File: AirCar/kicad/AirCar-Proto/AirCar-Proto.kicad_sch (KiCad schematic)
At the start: 6 parts, among them J1 Conn_01x05, J2 Barrel_Jack, J3 Conn_01x05, SW1 SW_Push, SW2 SW_SPDT, U1 Pico

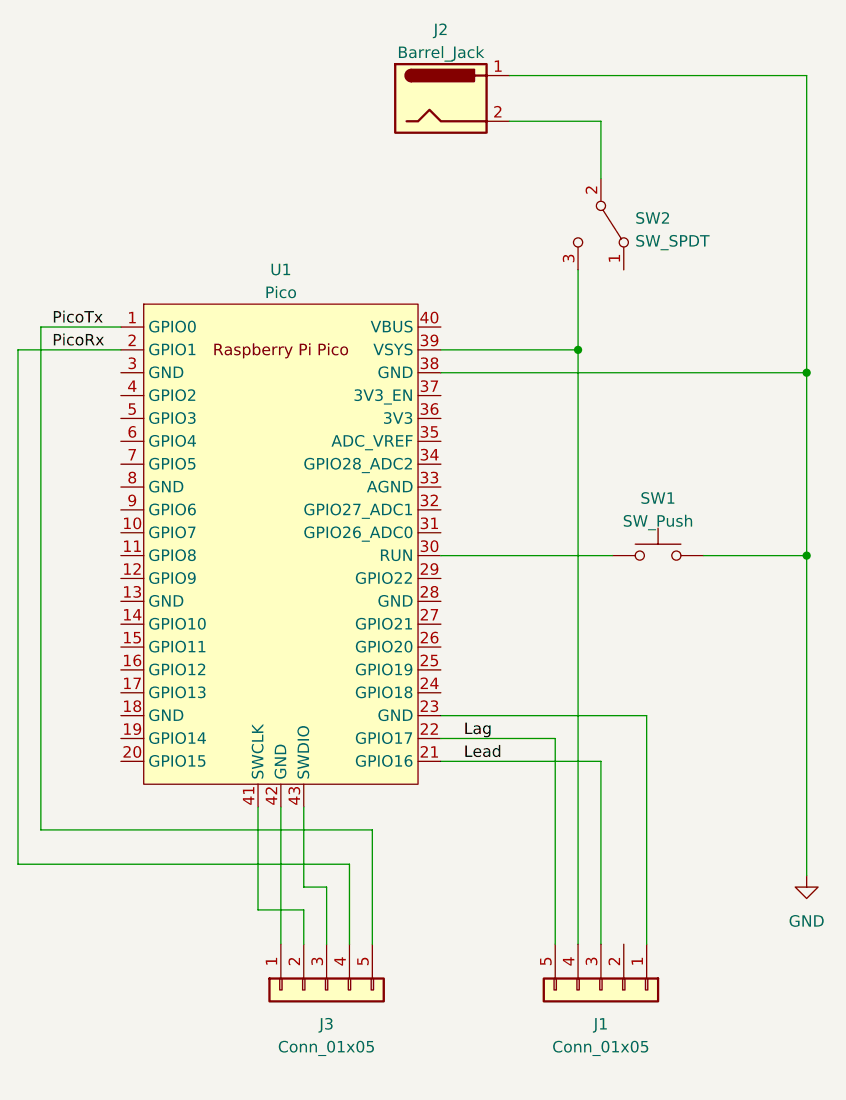
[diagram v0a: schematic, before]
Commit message: Add rudimentary schematic for proto-board version.
Note:  This schematic runs the rotary encoder below it's minimum
VDD value.  It seems to work fine (as it should), but it may be
flaky.

This fixes a bug in the stateUpdate logic that manifests when the
lead pin is higher (pin number) than the lag pin.
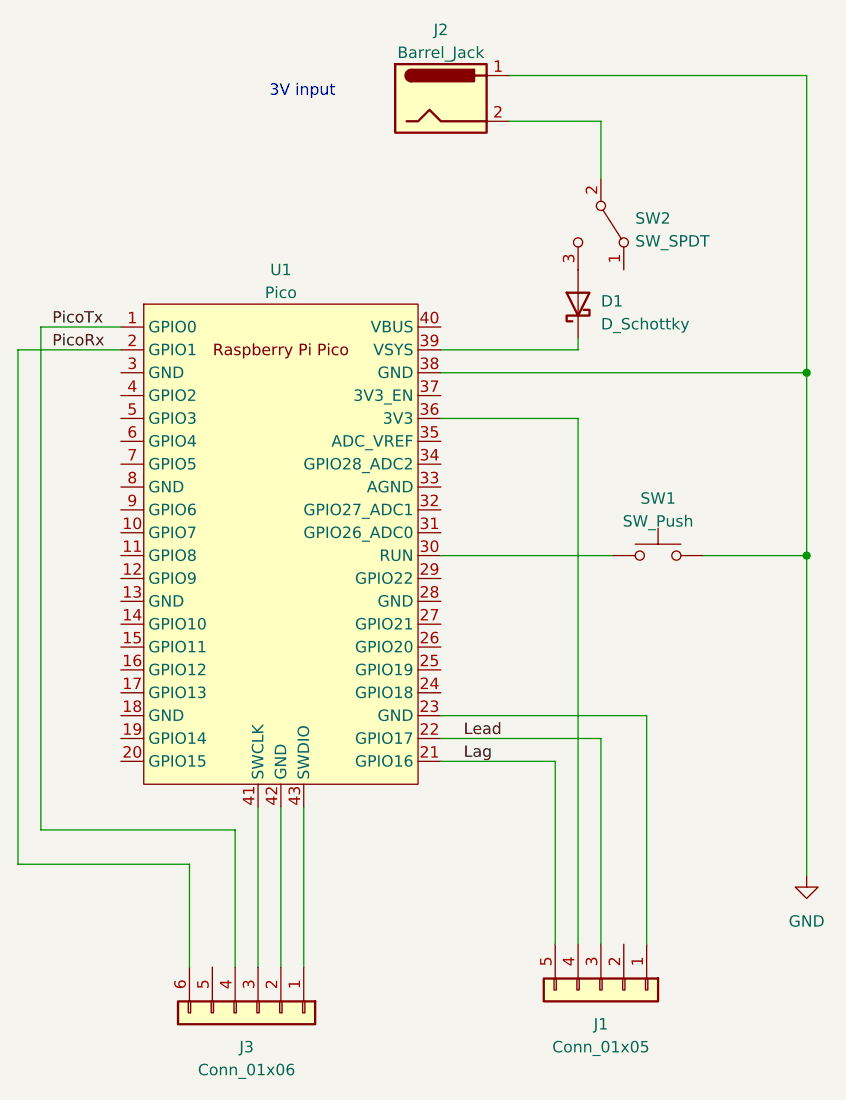
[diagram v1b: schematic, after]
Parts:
- removed J3: Conn_01x05, symbol Connector_Generic:Conn_01x05
- added D1: D_Schottky, symbol Device:D_Schottky
- added J3: Conn_01x06, symbol Connector_Generic:Conn_01x06
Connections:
- net Lag: now also U1.21 (GPIO16); no longer U1.22 (GPIO17)
- net Lead: now also U1.22 (GPIO17); no longer U1.21 (GPIO16)
- net PicoRx: now also J3.6 (Pin_6)
- net PicoTx: now also J3.4 (Pin_4)
- net at U1.36 (3V3): now also J1.4 (Pin_4)
- net at U1.41 (SWCLK): now also J3.3 (Pin_3)
- net at U1.42 (GND): now also J3.2 (Pin_2)
- net at U1.43 (SWDIO): now also J3.1 (Pin_1)
- new net: D1.2 (A), SW2.3 (C)
- new net: D1.1 (K), U1.39 (VSYS)
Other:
- note added: "3V input"
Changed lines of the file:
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@@
   (junction (at 236.22 83.82) (diameter 0) (color 0 0 0 0)
   )
-  (junction (at 210.82 60.96) (diameter 0) (color 0 0 0 0)
-  )
   (wire (pts (xy 213.36 35.56) (xy 213.36 41.91))
     (stroke (width 0) (type default))
   )
-  (wire (pts (xy 180.34 127) (xy 180.34 123.19))
-    (stroke (width 0) (type default))
-  )
-  (wire (pts (xy 180.34 123.19) (xy 175.26 123.19))
-    (stroke (width 0) (type default))
-  )
-  (wire (pts (xy 187.96 114.3) (xy 151.13 114.3))
-    (stroke (width 0) (type default))
-  )
-  (wire (pts (xy 182.88 120.65) (xy 180.34 120.65))
-    (stroke (width 0) (type default))
-  )
-  (wire (pts (xy 180.34 120.65) (xy 180.34 111.76))
+  (wire (pts (xy 195.58 106.68) (xy 208.28 106.68))
+    (stroke (width 0) (type default))
+  )
+  (wire (pts (xy 148.59 118.11) (xy 167.64 118.11))
+    (stroke (width 0) (type default))
+  )
+  (wire (pts (xy 180.34 111.76) (xy 180.34 129.54))
     (stroke (width 0) (type default))
   )
@@
     (stroke (width 0) (type default))
   )
-  (wire (pts (xy 187.96 127) (xy 187.96 114.3))
+  (wire (pts (xy 151.13 114.3) (xy 172.72 114.3))
     (stroke (width 0) (type default))
   )
@@
     (stroke (width 0) (type default))
   )
-  (wire (pts (xy 185.42 118.11) (xy 185.42 127))
-    (stroke (width 0) (type default))
-  )
   (wire (pts (xy 203.2 30.48) (xy 236.22 30.48))
     (stroke (width 0) (type default))
@@
     (stroke (width 0) (type default))
   )
-  (wire (pts (xy 213.36 127) (xy 213.36 106.68))
-    (stroke (width 0) (type default))
-  )
-  (wire (pts (xy 175.26 123.19) (xy 175.26 111.76))
-    (stroke (width 0) (type default))
-  )
-  (wire (pts (xy 208.28 104.14) (xy 208.28 127))
+  (wire (pts (xy 213.36 104.14) (xy 213.36 127))
+    (stroke (width 0) (type default))
+  )
+  (wire (pts (xy 213.36 104.14) (xy 195.58 104.14))
+    (stroke (width 0) (type default))
+  )
+  (wire (pts (xy 175.26 111.76) (xy 175.26 129.54))
     (stroke (width 0) (type default))
   )
@@
     (stroke (width 0) (type default))
   )
-  (wire (pts (xy 195.58 106.68) (xy 213.36 106.68))
-    (stroke (width 0) (type default))
-  )
-  (wire (pts (xy 208.28 104.14) (xy 195.58 104.14))
+  (wire (pts (xy 210.82 59.69) (xy 210.82 60.96))
     (stroke (width 0) (type default))
   )
@@
     (stroke (width 0) (type default))
   )
+  (wire (pts (xy 195.58 68.58) (xy 210.82 68.58))
+    (stroke (width 0) (type default))
+  )
   (wire (pts (xy 218.44 101.6) (xy 195.58 101.6))
     (stroke (width 0) (type default))
   )
-  (wire (pts (xy 177.8 111.76) (xy 177.8 127))
-    (stroke (width 0) (type default))
-  )
-  (wire (pts (xy 210.82 127) (xy 210.82 60.96))
-    (stroke (width 0) (type default))
-  )
-  (wire (pts (xy 182.88 127) (xy 182.88 120.65))
-    (stroke (width 0) (type default))
-  )
-  (wire (pts (xy 185.42 118.11) (xy 148.59 118.11))
+  (wire (pts (xy 177.8 111.76) (xy 177.8 129.54))
+    (stroke (width 0) (type default))
+  )
+  (wire (pts (xy 210.82 127) (xy 210.82 68.58))
+    (stroke (width 0) (type default))
+  )
+  (wire (pts (xy 167.64 118.11) (xy 167.64 129.54))
+    (stroke (width 0) (type default))
+  )
+  (wire (pts (xy 172.72 114.3) (xy 172.72 129.54))
     (stroke (width 0) (type default))
   )
@@
     (stroke (width 0) (type default))
   )
-  (wire (pts (xy 210.82 52.07) (xy 210.82 60.96))
-    (stroke (width 0) (type default))
-  )
   (wire (pts (xy 151.13 114.3) (xy 151.13 58.42))
     (stroke (width 0) (type default))
   )
-  (label "Lead" (at 198.12 106.68 0) (fields_autoplaced)
-    (effects (font (size 1.27 1.27)) (justify left bottom))
-  )
-  (label "Lag" (at 198.12 104.14 0) (fields_autoplaced)
+  (wire (pts (xy 208.28 106.68) (xy 208.28 127))
+    (stroke (width 0) (type default))
+  )
+  (text "3V input" (at 176.53 33.02 0)
+    (effects (font (size 1.27 1.27)) (justify left bottom))
+  )
+  (label "Lead" (at 198.12 104.14 0) (fields_autoplaced)
+    (effects (font (size 1.27 1.27)) (justify left bottom))
+  )
+  (label "Lag" (at 198.12 106.68 0) (fields_autoplaced)
     (effects (font (size 1.27 1.27)) (justify left bottom))
   )
@@
         (path "/8546dc3d-c898-4c7c-94a1-b884e04ce4f1"
           (reference "SW2") (unit 1)
+        )
+      )
+    )
+  )
+  (symbol (lib_id "Connector_Generic:Conn_01x06") (at 175.26 134.62 270) (unit 1)
+    (in_bom yes) (on_board yes) (dnp no) (fields_autoplaced)
+    (property "Reference" "J3" (at 173.99 138.43 90)
+      (effects (font (size 1.27 1.27)))
+    )
+    (property "Value" "Conn_01x06" (at 173.99 140.97 90)
+      (effects (font (size 1.27 1.27)))
+    )
+    (property "Footprint" "" (at 175.26 134.62 0)
+      (effects (font (size 1.27 1.27)) hide)
+    )
+    (property "Datasheet" "~" (at 175.26 134.62 0)
+      (effects (font (size 1.27 1.27)) hide)
+    )
+    (pin "1")
+    (pin "2")
+    (pin "3")
+    (pin "4")
+    (pin "5")
+    (pin "6")
+    (instances
+      (project "AirCar-Proto"
+        (path "/8546dc3d-c898-4c7c-94a1-b884e04ce4f1"
+          (reference "J3") (unit 1)
         )
       )
@@
     )
   )
+  (symbol (lib_id "Device:D_Schottky") (at 210.82 55.88 90) (unit 1)
+    (in_bom yes) (on_board yes) (dnp no) (fields_autoplaced)
+    (property "Reference" "D1" (at 213.36 55.5625 90)
+      (effects (font (size 1.27 1.27)) (justify right))
+    )
+    (property "Value" "D_Schottky" (at 213.36 58.1025 90)
+      (effects (font (size 1.27 1.27)) (justify right))
+    )
+    (property "Footprint" "" (at 210.82 55.88 0)
+      (effects (font (size 1.27 1.27)) hide)
+    )
+    (property "Datasheet" "~" (at 210.82 55.88 0)
+      (effects (font (size 1.27 1.27)) hide)
+    )
+    (pin "1")
+    (pin "2")
+    (instances
+      (project "AirCar-Proto"
+        (path "/8546dc3d-c898-4c7c-94a1-b884e04ce4f1"
+          (reference "D1") (unit 1)
+        )
+      )
+    )
+  )
   (symbol (lib_id "power:GND") (at 236.22 119.38 0) (unit 1)
     (in_bom yes) (on_board yes) (dnp no) (fields_autoplaced)
@@
         )
       )
-    )
-  )
-  (symbol (lib_id "Connector_Generic:Conn_01x05") (at 182.88 132.08 90) (mirror x) (unit 1)
-    (in_bom yes) (on_board yes) (dnp no) (fields_autoplaced)
-    (property "Reference" "J3" (at 182.88 135.89 90)
-      (effects (font (size 1.27 1.27)))
-    )
-    (property "Value" "Conn_01x05" (at 182.88 138.43 90)
-      (effects (font (size 1.27 1.27)))
-    )
-    (property "Footprint" "" (at 182.88 132.08 0)
-      (effects (font (size 1.27 1.27)) hide)
-    )
-    (property "Datasheet" "~" (at 182.88 132.08 0)
-      (effects (font (size 1.27 1.27)) hide)
-    )
-    (pin "1")
-    (pin "2")
-    (pin "3")
-    (pin "4")
-    (pin "5")
-    (instances
-      (project "AirCar-Proto"
-        (path "/8546dc3d-c898-4c7c-94a1-b884e04ce4f1"
-          (reference "J3") (unit 1)
-        )
-      )

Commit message: start working on board
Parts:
- added SW3: SW_Push, Library:SW4_1825910-B_TEC, symbol Switch:SW_Push
- D1: footprint (none) -> Diode_THT:D_DO-201AD_P12.70mm_Horizontal; Digikey (none) -> 1655-1922-1-ND
- J1: footprint (none) -> Connector_PinHeader_2.54mm:PinHeader_1x05_P2.54mm_Horizontal; Digikey (none) -> WM4903-ND
- J3: footprint (none) -> Connector_PinHeader_2.54mm:PinHeader_1x06_P2.54mm_Vertical
- SW1: footprint (none) -> Library:SW4_1825910-B_TEC; Digikey (none) -> 450-1650-ND
- SW2: footprint (none) -> Library:CS12ANW03_NKK; Digikey (none) -> 360-2131-ND
- U1: footprint RPi_Pico:RPi_Pico_SMD_TH -> MCU_RaspberryPi_and_Boards:RPi_Pico_SMD_TH
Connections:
- net GND: now also J1.1 (Pin_1), J3.2 (Pin_2), U1.18 (GND), U1.23 (GND), U1.28 (GND), U1.3 (GND), U1.33 (AGND), U1.42 (GND), U1.8 (GND), SW3.1
- net at U1.26 (GPIO20): now also SW3.2
- net VSYS: now reaches D1.1 (K), U1.39 (VSYS)
- no-connect marks 0 -> 28

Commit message: work on proto
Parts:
- removed SW1, SW3: SW_Push, Library:SW4_1825910-B_TEC, symbol Switch:SW_Push
- added H1, H2, H3, H4: MountingHole, MountingHole:MountingHole_3.2mm_M3, symbol Mechanical:MountingHole
- D1: footprint Diode_THT:D_DO-201AD_P12.70mm_Horizontal -> Diode_THT:D_DO-41_SOD81_P7.62mm_Horizontal; Digikey 1655-1922-1-ND -> 1N5817-E3/54GITR-ND
- J2: footprint (none) -> Connector_BarrelJack:BarrelJack_CUI_PJ-102AH_Horizontal; Digikey (none) -> PJ-102AH
- J3: footprint Connector_PinHeader_2.54mm:PinHeader_1x06_P2.54mm_Vertical -> Connector_PinHeader_2.54mm:PinHeader_1x06_P2.54mm_Horizontal
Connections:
- net V9P0: now reaches SW2.1 (A)
- net at SW2.3 (C): no longer D1.2 (A)
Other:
- note added: "9V input"
- note added: "Add switches Add 9V-5V reg Drive 5V onto sys. Encoder supposed to run on 5V Should probably provide an option to run on 5 or 3.3. Resistive divider probably OK on inputs. Get a three terminal barrel jack sym/footprint that actually matches what we are using."
- note removed: "3V input"
- moved on the sheet: J2, SW2

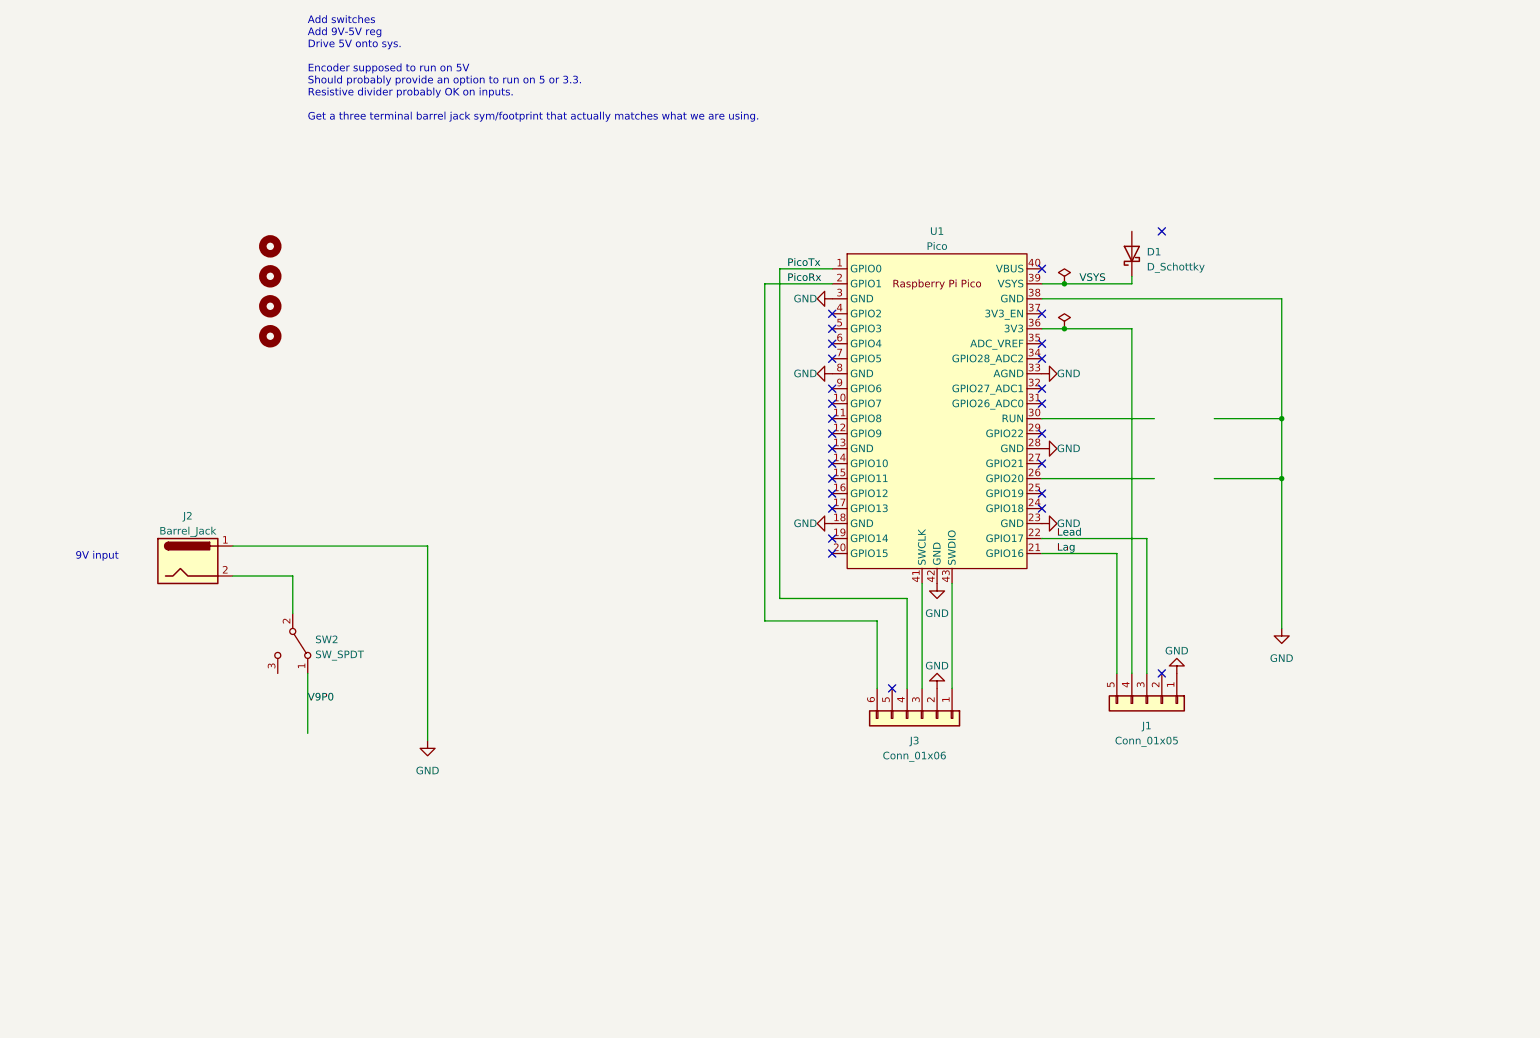
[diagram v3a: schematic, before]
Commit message: Good start.
Need to add 3v/5v option for encoder.
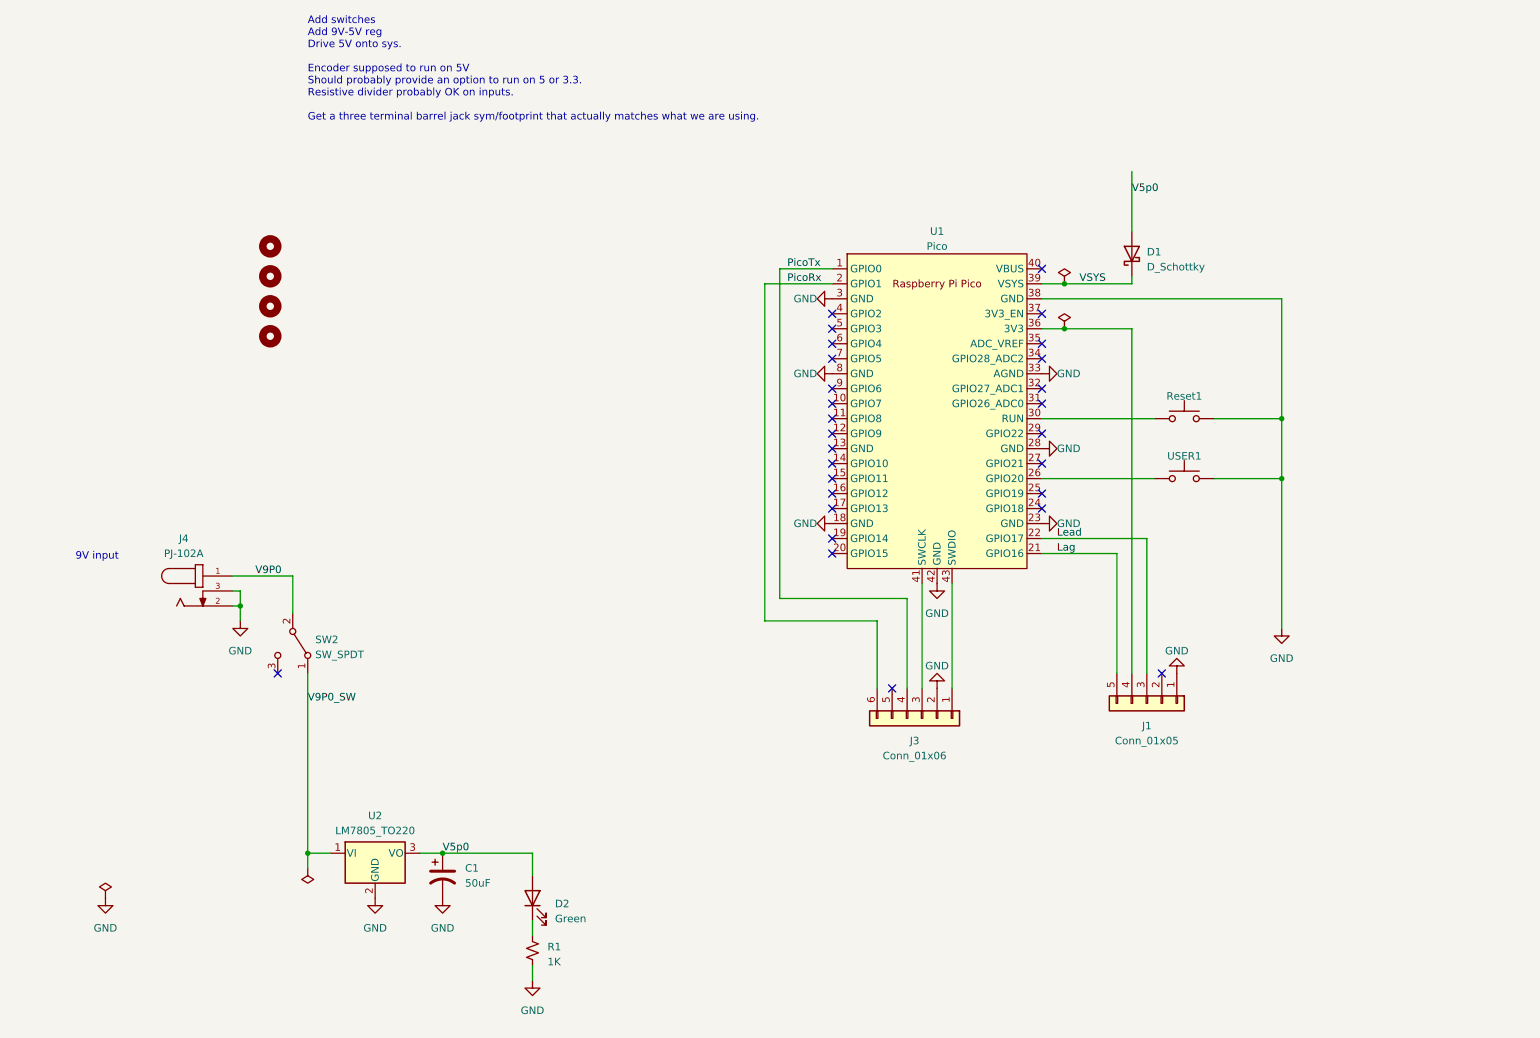
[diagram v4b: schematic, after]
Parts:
- removed J2: Barrel_Jack, Connector_BarrelJack:BarrelJack_CUI_PJ-102AH_Horizontal, symbol Connector:Barrel_Jack
- added C1: 50uF, Capacitor_THT:CP_Radial_D8.0mm_P2.50mm, symbol Device:C_Polarized_US
- added D2: Green, LED_THT:LED_D5.0mm, symbol Device:LED
- added J4: PJ-102A, Connector_BarrelJack:BarrelJack_CUI_PJ-102AH_Horizontal, symbol Local:PJ-102A
- added R1: 1K, Resistor_THT:R_Axial_DIN0207_L6.3mm_D2.5mm_P10.16mm_Horizontal, symbol Device:R_Small_US
- added Reset1, USER1: SmallPushbutton, Library:SW4_1825910-B_TEC, symbol Local:SmallPushbutton
- added U2: LM7805_TO220, Package_TO_SOT_THT:TO-220-3_Vertical, symbol Regulator_Linear:LM7805_TO220
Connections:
- net GND: now also C1.2, J4.2, J4.3, R1.2, Reset1.3, Reset1.4, U2.2 (GND), USER1.3, USER1.4
- net V9P0: now also SW2.2 (B), J4.1; no longer SW2.1 (A)
- net at U1.26 (GPIO20): now also USER1.1, USER1.2
- net at U1.30 (RUN): now also Reset1.1, Reset1.2
- net V5p0: now reaches D1.2 (A)
- net V5p0: now also C1.1, D2.2 (A), U2.3 (VO)
- new net: D2.1 (K), R1.1
- new net V9P0_SW: SW2.1 (A), U2.1 (VI)
